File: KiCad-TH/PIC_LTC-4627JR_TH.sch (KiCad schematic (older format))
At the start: 16 parts

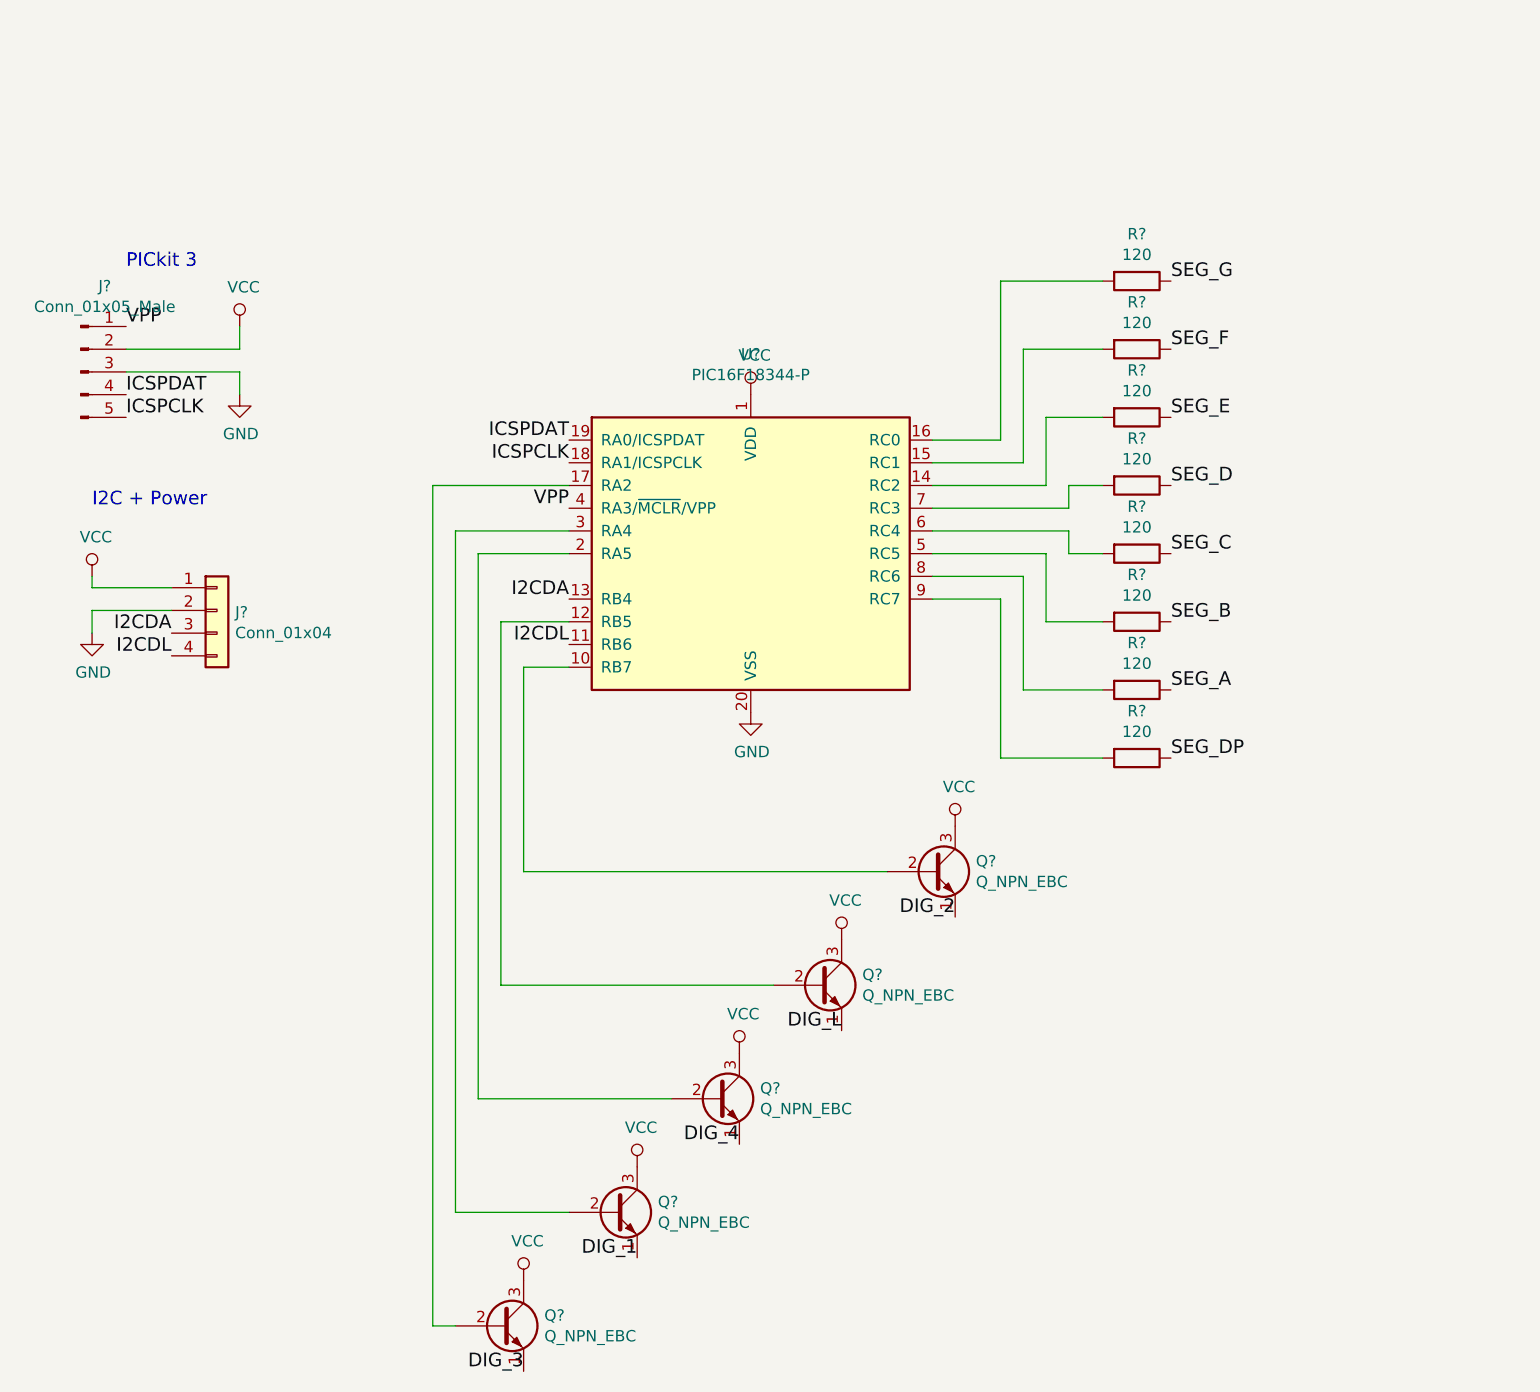
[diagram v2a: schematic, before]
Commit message: Add and wire custom LTC-4627JR to complete schematic
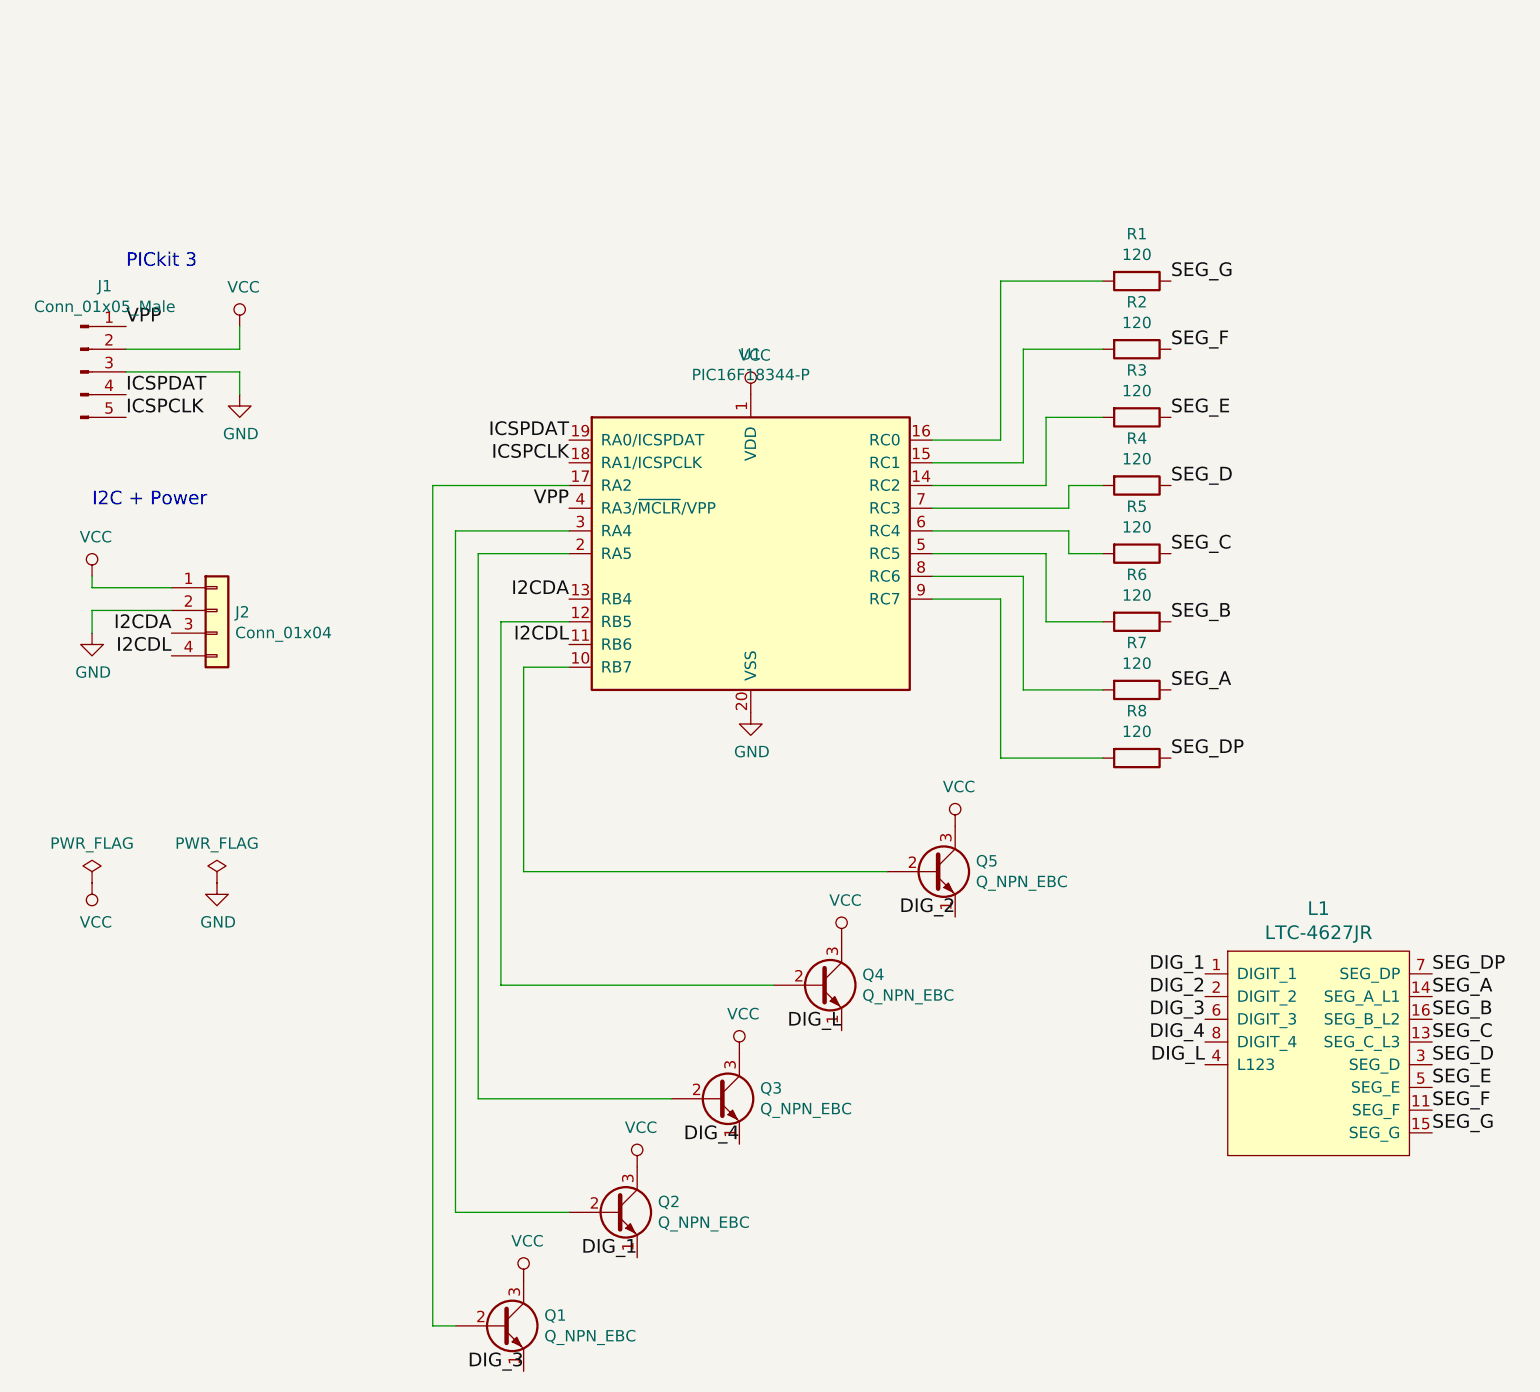
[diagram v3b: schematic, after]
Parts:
- added L1: LTC-4627JR, symbol LTC-4627JR
- gave numbers to parts that had none: 16
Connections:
- net DIG_1: now also L1.1 (DIGIT_1)
- net DIG_2: now also L1.2 (DIGIT_2)
- net DIG_3: now also L1.6 (DIGIT_3)
- net DIG_4: now also L1.8 (DIGIT_4)
- net DIG_L: now also L1.4 (L123)
- net SEG_A: now also L1.14 (SEG_A_L1)
- net SEG_B: now also L1.16 (SEG_B_L2)
- net SEG_C: now also L1.13 (SEG_C_L3)
- net SEG_D: now also L1.3 (SEG_D)
- net SEG_DP: now also L1.7 (SEG_DP)
- net SEG_E: now also L1.5 (SEG_E)
- net SEG_F: now also L1.11 (SEG_F)
- net SEG_G: now also L1.15 (SEG_G)
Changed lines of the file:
@@
 LIBS:valves
 LIBS:microchip_pic16mcu
-LIBS:leds
+LIBS:ltc-4627jr
 LIBS:PIC_LTC-4627JR_TH-cache
 EELAYER 26 0
@@
 $EndDescr
 $Comp
-L Conn_01x05_Male J?
+L Conn_01x05_Male J1
 U 1 1 59CC3EBA
 P 1250 2500
-F 0 "J?" H 1356 2878 50  0000 C CNN
+F 0 "J1" H 1356 2878 50  0000 C CNN
 F 1 "Conn_01x05_Male" H 1356 2787 50  0000 C CNN
 F 2 "" H 1250 2500 50  0001 C CNN
@@
 $EndComp
 $Comp
-L Conn_01x04 J?
+L Conn_01x04 J2
 U 1 1 59CC41F4
 P 1850 3550
-F 0 "J?" H 1930 3542 50  0000 L CNN
+F 0 "J2" H 1930 3542 50  0000 L CNN
 F 1 "Conn_01x04" H 1930 3451 50  0000 L CNN
 F 2 "" H 1850 3550 50  0001 C CNN
@@
 $EndComp
 $Comp
-L PIC16F18344-P U?
+L PIC16F18344-P U1
 U 1 1 59CC449B
 P 4200 3300
-F 0 "U?" H 4200 4178 50  0000 C CNN
+F 0 "U1" H 4200 4178 50  0000 C CNN
 F 1 "PIC16F18344-P" H 4200 4087 50  0000 C CNN
 F 2 "Housings_DIP:DIP-20_W7.62mm" H 4200 2520 50  0001 C CNN
@@
 $EndComp
 $Comp
-L R R?
+L R R1
 U 1 1 59CC458F
 P 5900 2100
-F 0 "R?" V 5693 2100 50  0000 C CNN
+F 0 "R1" V 5693 2100 50  0000 C CNN
 F 1 "120" V 5784 2100 50  0000 C CNN
 F 2 "" V 5830 2100 50  0001 C CNN
@@
 $EndComp
 $Comp
-L Q_NPN_EBC Q?
+L Q_NPN_EBC Q5
 U 1 1 59CC48C7
 P 5000 4700
-F 0 "Q?" H 5191 4746 50  0000 L CNN
+F 0 "Q5" H 5191 4746 50  0000 L CNN
 F 1 "Q_NPN_EBC" H 5191 4655 50  0000 L CNN
 F 2 "" H 5200 4800 50  0001 C CNN
@@
 ICSPCLK
 $Comp
-L VCC #PWR?
+L VCC #PWR010
 U 1 1 59CC4DA4
 P 4200 2600
-F 0 "#PWR?" H 4200 2450 50  0001 C CNN
+F 0 "#PWR010" H 4200 2450 50  0001 C CNN
 F 1 "VCC" H 4217 2773 50  0000 C CNN
 F 2 "" H 4200 2600 50  0001 C CNN
@@
 $EndComp
 $Comp
-L GND #PWR?
+L GND #PWR011
 U 1 1 59CC4E1B
 P 4200 4000
-F 0 "#PWR?" H 4200 3750 50  0001 C CNN
+F 0 "#PWR011" H 4200 3750 50  0001 C CNN
 F 1 "GND" H 4205 3827 50  0000 C CNN
 F 2 "" H 4200 4000 50  0001 C CNN
@@
 ICSPCLK
 $Comp
-L VCC #PWR?
+L VCC #PWR05
 U 1 1 59CC4F24
 P 1950 2300
-F 0 "#PWR?" H 1950 2150 50  0001 C CNN
+F 0 "#PWR05" H 1950 2150 50  0001 C CNN
 F 1 "VCC" H 1967 2473 50  0000 C CNN
 F 2 "" H 1950 2300 50  0001 C CNN
@@
 $EndComp
 $Comp
-L GND #PWR?
+L GND #PWR06
 U 1 1 59CC4F5C
 P 1950 2600
-F 0 "#PWR?" H 1950 2350 50  0001 C CNN
+F 0 "#PWR06" H 1950 2350 50  0001 C CNN
 F 1 "GND" H 1955 2427 50  0000 C CNN
 F 2 "" H 1950 2600 50  0001 C CNN
@@
 	1950 2400 1950 2300
 $Comp
-L VCC #PWR?
+L VCC #PWR01
 U 1 1 59CC4FA4
 P 1300 3400
-F 0 "#PWR?" H 1300 3250 50  0001 C CNN
+F 0 "#PWR01" H 1300 3250 50  0001 C CNN
 F 1 "VCC" H 1317 3573 50  0000 C CNN
 F 2 "" H 1300 3400 50  0001 C CNN
@@
 $EndComp
 $Comp
-L GND #PWR?
+L GND #PWR02
 U 1 1 59CC4FE1
 P 1300 3650
-F 0 "#PWR?" H 1300 3400 50  0001 C CNN
+F 0 "#PWR02" H 1300 3400 50  0001 C CNN
 F 1 "GND" H 1305 3477 50  0000 C CNN
 F 2 "" H 1300 3650 50  0001 C CNN
@@
 I2C + Power
 $Comp
-L R R?
+L R R2
 U 1 1 59CC547E
 P 5900 2400
-F 0 "R?" V 5693 2400 50  0000 C CNN
+F 0 "R2" V 5693 2400 50  0000 C CNN
 F 1 "120" V 5784 2400 50  0000 C CNN
 F 2 "" V 5830 2400 50  0001 C CNN
@@
 $EndComp
 $Comp
-L R R?
+L R R3
 U 1 1 59CC54A2
 P 5900 2700
-F 0 "R?" V 5693 2700 50  0000 C CNN
+F 0 "R3" V 5693 2700 50  0000 C CNN
 F 1 "120" V 5784 2700 50  0000 C CNN
 F 2 "" V 5830 2700 50  0001 C CNN
@@
 $EndComp
 $Comp
-L R R?
+L R R4
 U 1 1 59CC54C8
 P 5900 3000
-F 0 "R?" V 5693 3000 50  0000 C CNN
+F 0 "R4" V 5693 3000 50  0000 C CNN
 F 1 "120" V 5784 3000 50  0000 C CNN
 F 2 "" V 5830 3000 50  0001 C CNN
@@
 $EndComp
 $Comp
-L R R?
+L R R5
 U 1 1 59CC54F0
 P 5900 3300
-F 0 "R?" V 5693 3300 50  0000 C CNN
+F 0 "R5" V 5693 3300 50  0000 C CNN
 F 1 "120" V 5784 3300 50  0000 C CNN
 F 2 "" V 5830 3300 50  0001 C CNN
@@
 $EndComp
 $Comp
-L R R?
+L R R6
 U 1 1 59CC551A
 P 5900 3600
-F 0 "R?" V 5693 3600 50  0000 C CNN
+F 0 "R6" V 5693 3600 50  0000 C CNN
 F 1 "120" V 5784 3600 50  0000 C CNN
 F 2 "" V 5830 3600 50  0001 C CNN
@@
 $EndComp
 $Comp
-L R R?
+L R R7
 U 1 1 59CC555E
 P 5900 3900
-F 0 "R?" V 5693 3900 50  0000 C CNN
+F 0 "R7" V 5693 3900 50  0000 C CNN
 F 1 "120" V 5784 3900 50  0000 C CNN
 F 2 "" V 5830 3900 50  0001 C CNN
@@
 $EndComp
 $Comp
-L R R?
+L R R8
 U 1 1 59CC558C
 P 5900 4200
-F 0 "R?" V 5693 4200 50  0000 C CNN
+F 0 "R8" V 5693 4200 50  0000 C CNN
 F 1 "120" V 5784 4200 50  0000 C CNN
 F 2 "" V 5830 4200 50  0001 C CNN
@@
 SEG_DP
 $Comp
-L VCC #PWR?
+L VCC #PWR013
 U 1 1 59CC621C
 P 5100 4500
-F 0 "#PWR?" H 5100 4350 50  0001 C CNN
+F 0 "#PWR013" H 5100 4350 50  0001 C CNN
 F 1 "VCC" H 5117 4673 50  0000 C CNN
 F 2 "" H 5100 4500 50  0001 C CNN
@@
 $EndComp
 $Comp
-L Q_NPN_EBC Q?
+L Q_NPN_EBC Q4
 U 1 1 59CC63E8
 P 4500 5200
-F 0 "Q?" H 4691 5246 50  0000 L CNN
+F 0 "Q4" H 4691 5246 50  0000 L CNN
 F 1 "Q_NPN_EBC" H 4691 5155 50  0000 L CNN
 F 2 "" H 4700 5300 50  0001 C CNN
@@
 $EndComp
 $Comp
-L VCC #PWR?
+L VCC #PWR012
 U 1 1 59CC6438
 P 4600 5000
-F 0 "#PWR?" H 4600 4850 50  0001 C CNN
+F 0 "#PWR012" H 4600 4850 50  0001 C CNN
 F 1 "VCC" H 4617 5173 50  0000 C CNN
 F 2 "" H 4600 5000 50  0001 C CNN
@@
 $EndComp
 $Comp
-L VCC #PWR?
+L VCC #PWR09
 U 1 1 59CC6470
 P 4150 5500
-F 0 "#PWR?" H 4150 5350 50  0001 C CNN
+F 0 "#PWR09" H 4150 5350 50  0001 C CNN
 F 1 "VCC" H 4167 5673 50  0000 C CNN
 F 2 "" H 4150 5500 50  0001 C CNN
@@
 $EndComp
 $Comp
-L Q_NPN_EBC Q?
+L Q_NPN_EBC Q3
 U 1 1 59CC6495
 P 4050 5700
-F 0 "Q?" H 4241 5746 50  0000 L CNN
+F 0 "Q3" H 4241 5746 50  0000 L CNN
 F 1 "Q_NPN_EBC" H 4241 5655 50  0000 L CNN
 F 2 "" H 4250 5800 50  0001 C CNN
@@
 $EndComp
 $Comp
-L VCC #PWR?
+L VCC #PWR08
 U 1 1 59CC64CD
 P 3700 6000
-F 0 "#PWR?" H 3700 5850 50  0001 C CNN
+F 0 "#PWR08" H 3700 5850 50  0001 C CNN
 F 1 "VCC" H 3717 6173 50  0000 C CNN
 F 2 "" H 3700 6000 50  0001 C CNN
@@
 $EndComp
 $Comp
-L Q_NPN_EBC Q?
+L Q_NPN_EBC Q2
 U 1 1 59CC64F4
 P 3600 6200
-F 0 "Q?" H 3791 6246 50  0000 L CNN
+F 0 "Q2" H 3791 6246 50  0000 L CNN
 F 1 "Q_NPN_EBC" H 3791 6155 50  0000 L CNN
 F 2 "" H 3800 6300 50  0001 C CNN
@@
 	3000 5700 3850 5700
 $Comp
-L VCC #PWR?
+L VCC #PWR07
 U 1 1 59CC6D0F
 P 3200 6500
-F 0 "#PWR?" H 3200 6350 50  0001 C CNN
+F 0 "#PWR07" H 3200 6350 50  0001 C CNN
 F 1 "VCC" H 3217 6673 50  0000 C CNN
 F 2 "" H 3200 6500 50  0001 C CNN
@@
 $EndComp
 $Comp
-L Q_NPN_EBC Q?
+L Q_NPN_EBC Q1
 U 1 1 59CC6D38
 P 3100 6700
-F 0 "Q?" H 3291 6746 50  0000 L CNN
+F 0 "Q1" H 3291 6746 50  0000 L CNN
 F 1 "Q_NPN_EBC" H 3291 6655 50  0000 L CNN
 F 2 "" H 3300 6800 50  0001 C CNN
@@
 Text Label 3200 6900 2    60   ~ 0
 DIG_3
+$Comp
+L LTC-4627JR L1
+U 1 1 59CC84A7
+P 6700 4950
+F 0 "L1" H 6700 5037 60  0000 C CNN
+F 1 "LTC-4627JR" H 6700 4931 60  0000 C CNN
+F 2 "" H 6700 4950 60  0001 C CNN
+F 3 "" H 6700 4950 60  0001 C CNN
+	1    6700 4950
+	1    0    0    -1
+$EndComp
+Text Label 6200 5150 2    60   ~ 0
+DIG_1
+Text Label 6200 5250 2    60   ~ 0
+DIG_2
+Text Label 6200 5350 2    60   ~ 0
+DIG_3
+Text Label 6200 5450 2    60   ~ 0
+DIG_4
+Text Label 6200 5550 2    60   ~ 0
+DIG_L
+Text Label 7200 5150 0    60   ~ 0
+SEG_DP
+Text Label 7200 5250 0    60   ~ 0
+SEG_A
+Text Label 7200 5350 0    60   ~ 0
+SEG_B
+Text Label 7200 5450 0    60   ~ 0
+SEG_C
+Text Label 7200 5550 0    60   ~ 0
+SEG_D
+Text Label 7200 5650 0    60   ~ 0
+SEG_E
+Text Label 7200 5750 0    60   ~ 0
+SEG_F
+Text Label 7200 5850 0    60   ~ 0
+SEG_G
+$Comp
+L PWR_FLAG #FLG01
+U 1 1 59CC9227
+P 1300 4750
+F 0 "#FLG01" H 1300 4825 50  0001 C CNN
+F 1 "PWR_FLAG" H 1300 4924 50  0000 C CNN
+F 2 "" H 1300 4750 50  0001 C CNN
+F 3 "" H 1300 4750 50  0001 C CNN
+	1    1300 4750
+	1    0    0    -1
+$EndComp
+$Comp
+L VCC #PWR03
+U 1 1 59CC9283
+P 1300 4750
+F 0 "#PWR03" H 1300 4600 50  0001 C CNN
+F 1 "VCC" H 1317 4923 50  0000 C CNN
+F 2 "" H 1300 4750 50  0001 C CNN
+F 3 "" H 1300 4750 50  0001 C CNN
+	1    1300 4750
+	1    0    0    1
+$EndComp
+$Comp
+L PWR_FLAG #FLG02
+U 1 1 59CC9667
+P 1850 4750
+F 0 "#FLG02" H 1850 4825 50  0001 C CNN
+F 1 "PWR_FLAG" H 1850 4924 50  0000 C CNN
+F 2 "" H 1850 4750 50  0001 C CNN
+F 3 "" H 1850 4750 50  0001 C CNN
+	1    1850 4750
+	1    0    0    -1
+$EndComp
+$Comp
+L GND #PWR04
+U 1 1 59CC96C3
+P 1850 4750
+F 0 "#PWR04" H 1850 4500 50  0001 C CNN
+F 1 "GND" H 1855 4577 50  0000 C CNN
+F 2 "" H 1850 4750 50  0001 C CNN
+F 3 "" H 1850 4750 50  0001 C CNN
+	1    1850 4750
+	1    0    0    -1
+$EndComp
 $EndSCHEMATC
